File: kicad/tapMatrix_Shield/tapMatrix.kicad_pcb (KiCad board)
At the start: 2 copper layers, 121.9 x 80 mm, 24 parts, among them IC1 DS1307, P7 SPKR, U1 APE8865N-33-HF-3, U2 MCP4921-E/SN, U3 74LS125, U4 TL072

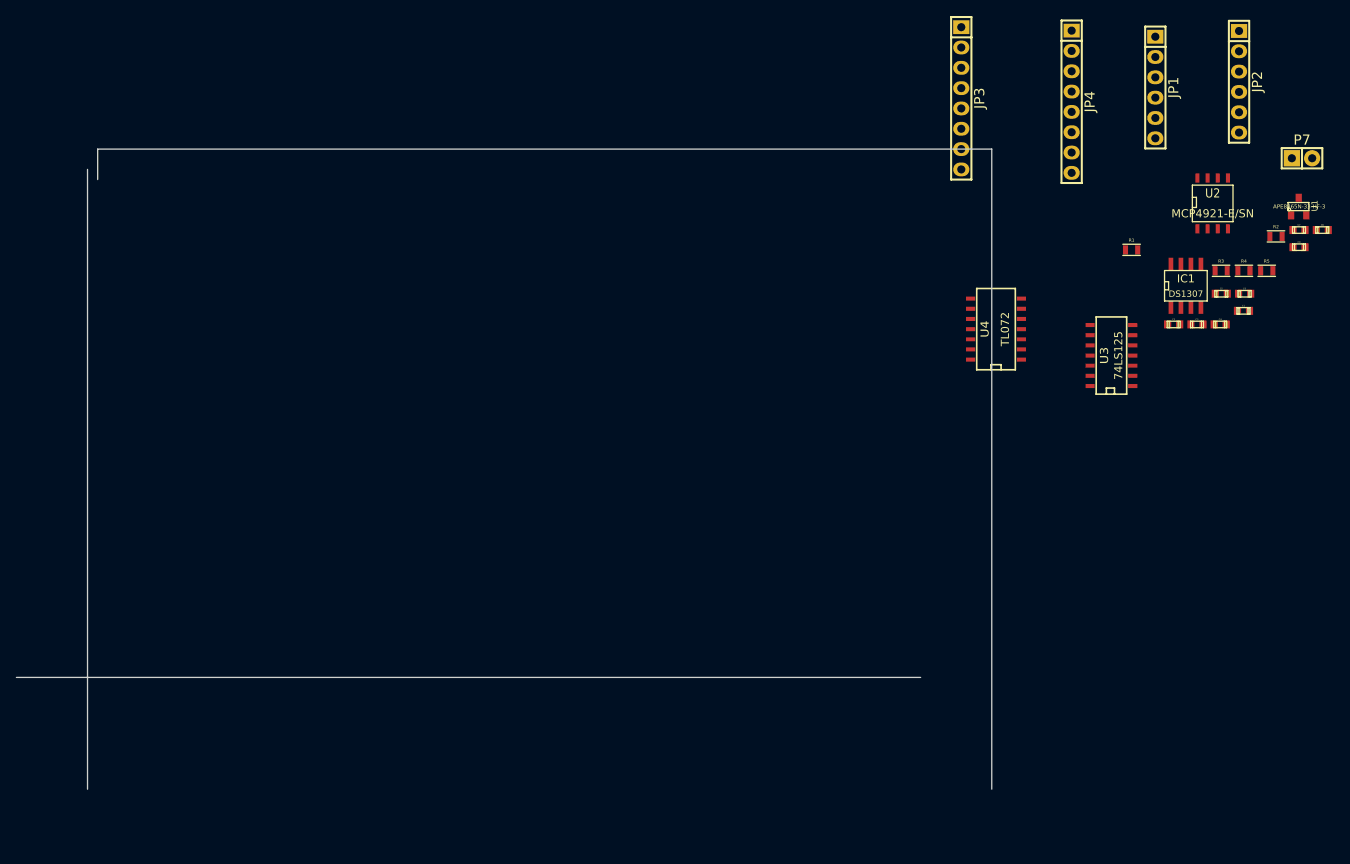
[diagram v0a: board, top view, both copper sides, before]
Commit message: added footprints for battery and ribbon sockets
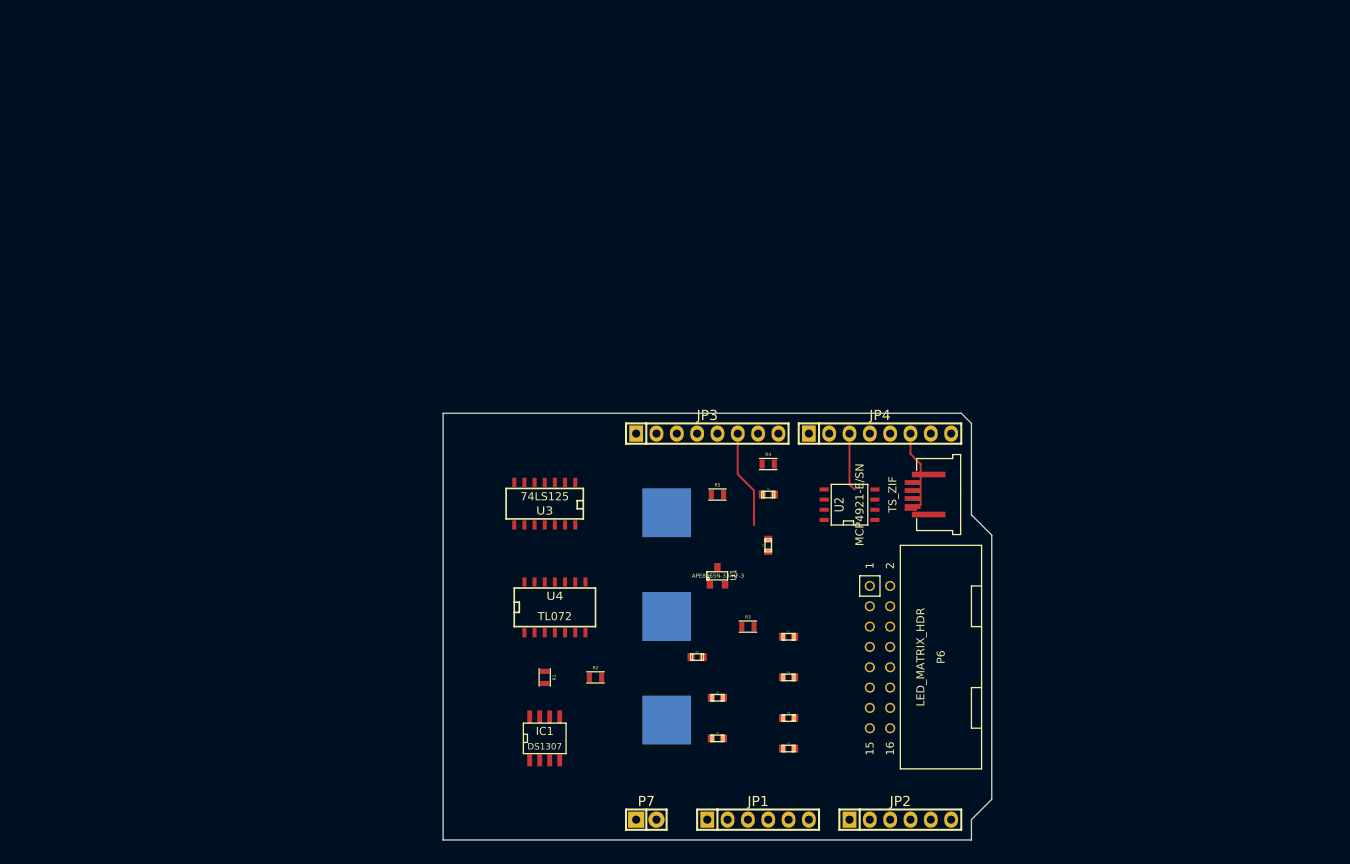
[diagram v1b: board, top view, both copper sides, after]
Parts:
- added BT1: BATTERY, tapmatrix:CR2032, B.Cu at (158.8, 111.8)
- added P5: TS_ZIF, tapmatrix:SFW4R­5STE1LF, F.Cu at (190.5, 96.5)
- added P6: LED_MATRIX_HDR, tapmatrix:5103310­-3, F.Cu at (185.4, 116.8)
- moved P7 116.4 mm to (156.2, 137.2)
- moved JP1 104.1 mm to (170.2, 137.2), turned to 0 degrees
- moved JP2 101.5 mm to (188.0, 137.2), turned to 0 degrees
- moved R2 101.4 mm to (149.9, 119.4)
- moved IC1 98.1 mm to (143.5, 127.0)
- moved C9 95.2 mm to (165.1, 127.0)
- moved R1 90.8 mm to (143.5, 119.4), turned to 270 degrees
- moved U1 86.1 mm to (165.1, 106.7)
- moved C6 83.0 mm to (165.1, 121.9)
- moved C5 79.7 mm to (162.6, 116.8)
- moved C7 77.2 mm to (171.4, 102.9), turned to 90 degrees
- moved C8 76.7 mm to (171.4, 96.5)
- moved R5 74.1 mm to (165.1, 96.5)
- moved R3 74.0 mm to (168.9, 113.0)
- moved U3 73.1 mm to (143.5, 97.8), turned to 180 degrees
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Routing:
- net /SD_CS: track 0.00 -> 12.3 mm
- net /XM: track 0.00 -> 9.04 mm
- net /DAC_LAT: track 0.00 -> 7.25 mm
- net /DAC_CS: track 0.00 -> 2.54 mm
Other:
- board size 121.9 x 80 mm -> 68.6 x 53.3 mm
- board text added: "3.3V"
- board text added: "5V"
- board text added: "Aref"
- board text added: "GND"
- board text added: "INT0"
- board text added: "INT1/PWM"
- board text added: "IOref"
- board text added: "MISO"
- board text added: "MOSI"
- board text added: "MOSI/PWM"
- board text added: "PWM"
- board text added: "RST"
- board text added: "Rx"
- board text added: "SCK"
- board text added: "SCK/LED"
- board text added: "SCL"
- board text added: "SDA"
- board text added: "SS/PWM"
- board text added: "Tx"
- board text added: "VTG"
- board text added: "Vin"

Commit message: created power and signal netclasses, updated design rules for oshpark
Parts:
- moved BT1 5.08 mm to (153.7, 111.8)
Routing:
- net /SD_CS: track 12.3 -> 0.00 mm
- net /DAC_LAT: track 7.25 -> 0.00 mm
- net /XM: track 9.04 -> 2.17 mm
- net /DAC_CS: track 2.54 -> 0.00 mm
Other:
- net class Power added: clearance 0.381, trace_width 0.762, via_dia 1.27, via_drill 0.889
- net class Signal added: clearance 0.1524, trace_width 0.254, via_dia 0.889, via_drill 0.635
- rule trace_min: 0.254 -> 0.1524
- rule via_min_drill: 0.508 -> 0.3302
- rule via_min_size: 0.889 -> 0.508
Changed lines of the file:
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@@
     (thickness 1.6)
     (drawings 96)
-    (tracks 10)
+    (tracks 2)
     (zones 0)
     (modules 27)
@@
   (setup
     (last_trace_width 0.254)
+    (user_trace_width 0.254)
+    (user_trace_width 0.3556)
+    (user_trace_width 0.508)
     (trace_clearance 0.254)
     (zone_clearance 0.508)
     (zone_45_only no)
-    (trace_min 0.254)
+    (trace_min 0.1524)
     (segment_width 0.2)
     (edge_width 0.1)
     (via_size 0.889)
     (via_drill 0.635)
-    (via_min_size 0.889)
-    (via_min_drill 0.508)
+    (via_min_size 0.508)
+    (via_min_drill 0.3302)
     (uvia_size 0.508)
     (uvia_drill 0.127)
     (uvias_allowed no)
-    (uvia_min_size 0.508)
-    (uvia_min_drill 0.127)
+    (uvia_min_size 0.381)
+    (uvia_min_drill 0.0127)
     (pcb_text_width 0.3)
     (pcb_text_size 1.5 1.5)
@@
     (uvia_dia 0.508)
     (uvia_drill 0.127)
+  )
+  (net_class Power ""
+    (clearance 0.381)
+    (trace_width 0.762)
+    (via_dia 1.27)
+    (via_drill 0.889)
+    (uvia_dia 0.508)
+    (uvia_drill 0.127)
     (add_net +3.3V)
     (add_net +5V)
+  )
+  (net_class Signal ""
+    (clearance 0.1524)
+    (trace_width 0.254)
+    (via_dia 0.889)
+    (via_drill 0.635)
+    (uvia_dia 0.508)
+    (uvia_drill 0.127)
     (add_net /CS)
     (add_net /DAC_CS)
@@
   )
   (module tapmatrix:CR2032 (layer B.Cu)
-    (at 158.75 111.76 270)
+    (at 153.67 111.76 270)
     (fp_text reference BT1 (at 0 -13.97 270) (layer B.SilkS)
       (effects (font (size 1 1) (thickness 0.15)) (justify mirror))
@@
   (module tapmatrix:SFW4R­5STE1LF (layer F.Cu)
     (at 190.5 96.52 90)
+    (clearance 0.1524)
     (fp_text reference P5 (at 0 7.5 90) (layer F.SilkS) hide
       (effects (font (size 1 1) (thickness 0.15)))
@@
   (gr_line (start 0 0) (end 66.04 0) (layer Dwgs.User) (width 0.1))
   (gr_line (start 0 0) (end 0 -53.34) (layer Dwgs.User) (width 0.1))
+  (segment (start 189.865 98.425) (end 188.595 98.425) (width 0.254) (layer F.Cu) (net 17))
   (segment (start 190.5 97.79) (end 189.865 98.425) (width 0.254) (layer F.Cu) (net 17))
-  (segment (start 190.5 92.71) (end 190.5 97.79) (width 0.254) (layer F.Cu) (net 17))
-  (segment (start 189.865 98.425) (end 188.595 98.425) (width 0.254) (layer F.Cu) (net 17))
-  (segment (start 189.23 91.44) (end 190.5 92.71) (width 0.254) (layer F.Cu) (net 17))
-  (segment (start 167.64 88.9) (end 167.64 93.98) (width 0.254) (layer F.Cu) (net 25))
-  (segment (start 169.672 96.012) (end 169.672 100.33) (width 0.254) (layer F.Cu) (net 25))
-  (segment (start 167.64 93.98) (end 169.672 96.012) (width 0.254) (layer F.Cu) (net 25))
-  (segment (start 181.61 88.9) (end 181.61 95.25) (width 0.254) (layer F.Cu) (net 30))
-  (segment (start 181.61 95.25) (end 182.245 95.885) (width 0.254) (layer F.Cu) (net 30))
-  (segment (start 189.23 88.9) (end 189.23 91.44) (width 0.254) (layer F.Cu) (net 33))
 )

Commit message: add microsd module
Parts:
- added U5: SD_CARD, tapmatrix:114-00841-68, F.Cu at (134.6, 87.6)
- moved P5 56.8 mm to (147.3, 133.3), turned to 0 degrees
- moved U3 14.0 mm to (157.5, 99.1), turned to 270 degrees
- moved R2 13.7 mm to (142.2, 108.0), turned to 270 degrees
- moved U4 12.8 mm to (157.5, 111.8), turned to 270 degrees
- moved R1 12.5 mm to (138.4, 108.0), turned to 0 degrees
- moved IC1 10.9 mm to (139.7, 116.8)
- moved U1 2.54 mm to (167.6, 106.7), turned to 180 degrees
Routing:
- net /XM: track 2.17 -> 0.00 mm
- net (no net): track 0.00 -> 2.17 mm

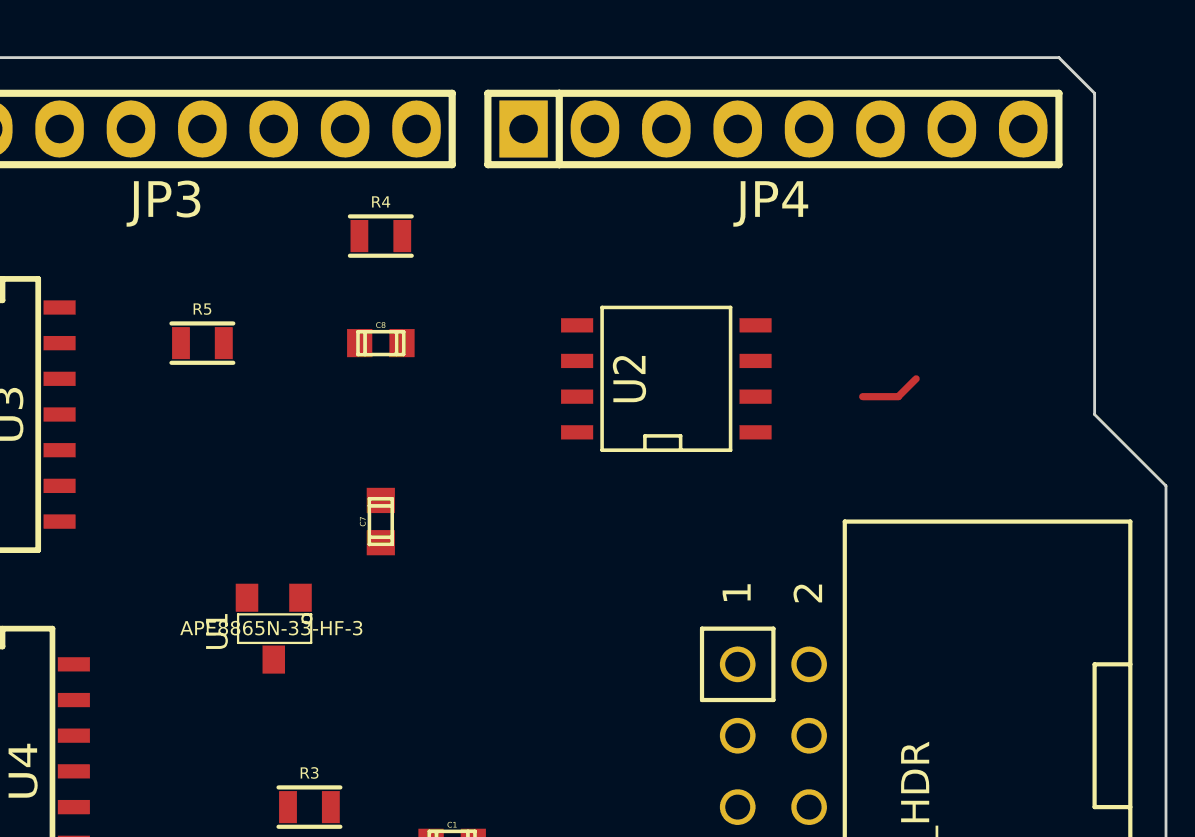
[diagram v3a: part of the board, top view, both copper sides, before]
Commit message: begin routing pcb
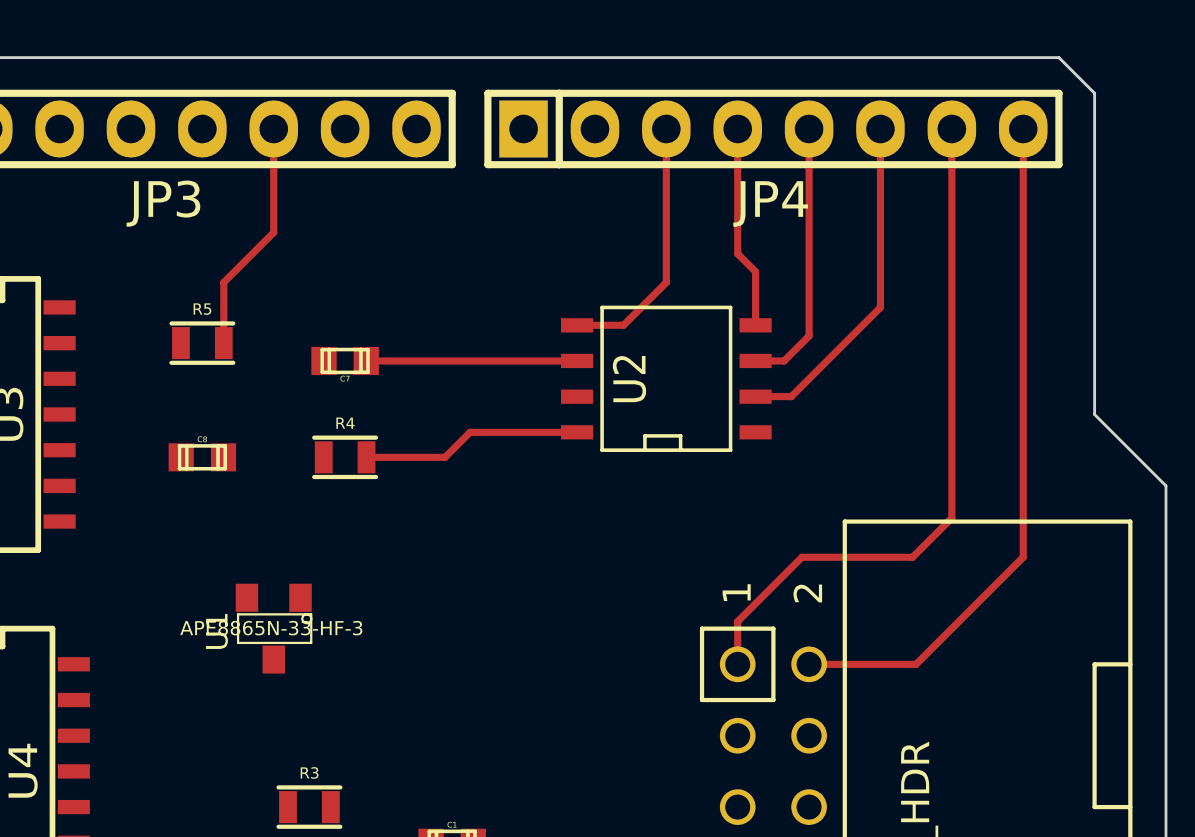
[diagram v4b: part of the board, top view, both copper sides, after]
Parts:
- moved R4 7.98 mm to (170.2, 100.6)
- moved C8 7.54 mm to (165.1, 100.6)
- moved C7 5.85 mm to (170.2, 97.2), turned to 180 degrees
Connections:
- net +3.3V renamed VCC
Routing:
- net /MATRIX_CS: track 0.00 -> 24.5 mm
- net /MATRIX_CLK: track 0.00 -> 24.4 mm
- net /DAC_CS: track 0.00 -> 12.1 mm
- net /DAC_SCK: track 0.00 -> 9.64 mm
- net /DAC_LAT: track 0.00 -> 9.27 mm
- net /SD_CS: track 0.00 -> 8.36 mm
- net Net-(R4-Pad2): track 0.00 -> 7.86 mm
- net Net-(C7-Pad2): track 0.00 -> 7.50 mm
- net /DAC_DI: track 0.00 -> 7.25 mm
- net (no net): track 2.17 -> 0.00 mm

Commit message: continue routing
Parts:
- moved C9 12.7 mm to (154.9, 119.4), turned to 180 degrees
- moved C5 3.86 mm to (166.4, 116.2)
- moved C6 2.84 mm to (166.4, 119.4)
- moved C2 2.16 mm to (174.0, 126.1)
- moved C3 1.90 mm to (174.0, 122.6)
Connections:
- U3 pad 6: /MISO -> /DATA_IN
- U5 pad 3: /MOSI -> /DATA_IN
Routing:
- net /I2C_SCL: track 0.00 -> 75.6 mm, vias 0 -> 2
- net VCC: track 0.00 -> 69.2 mm, vias 0 -> 2
- net /I2C_SDA: track 0.00 -> 68.6 mm
- net /YP: track 0.00 -> 50.0 mm
- net /XM: track 0.00 -> 48.7 mm
- net /YM: track 0.00 -> 47.6 mm
- net /XP: track 0.00 -> 47.1 mm, vias 0 -> 1
- net /MATRIX_DATA: track 0.00 -> 32.7 mm, vias 0 -> 2
- net /MATRIX_WR: track 0.00 -> 31.4 mm, vias 0 -> 2
- net Net-(BT1-Pad1): track 0.00 -> 31.2 mm, vias 0 -> 1
- net /MISO: track 0.00 -> 29.0 mm, vias 0 -> 1
- net /CS: track 0.00 -> 26.9 mm
- net Net-(C9-Pad2): track 0.00 -> 25.4 mm, vias 0 -> 2
- net /DATA_IN: track 0.00 -> 20.7 mm
- net /SCLK: track 0.00 -> 20.1 mm
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- added copper zone on F.Cu, net +5V
- added copper zone on B.Cu, net GND

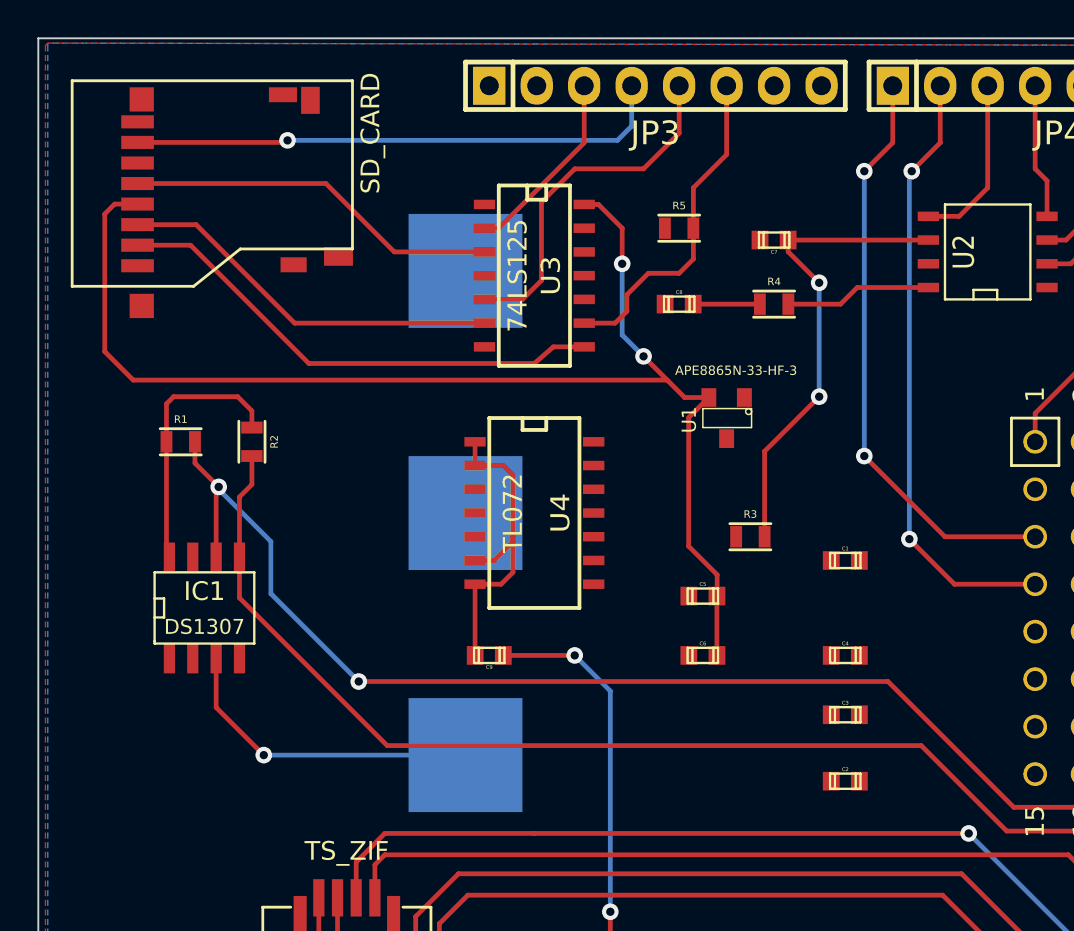
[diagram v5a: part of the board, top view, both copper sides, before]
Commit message: complete first attempt at routing
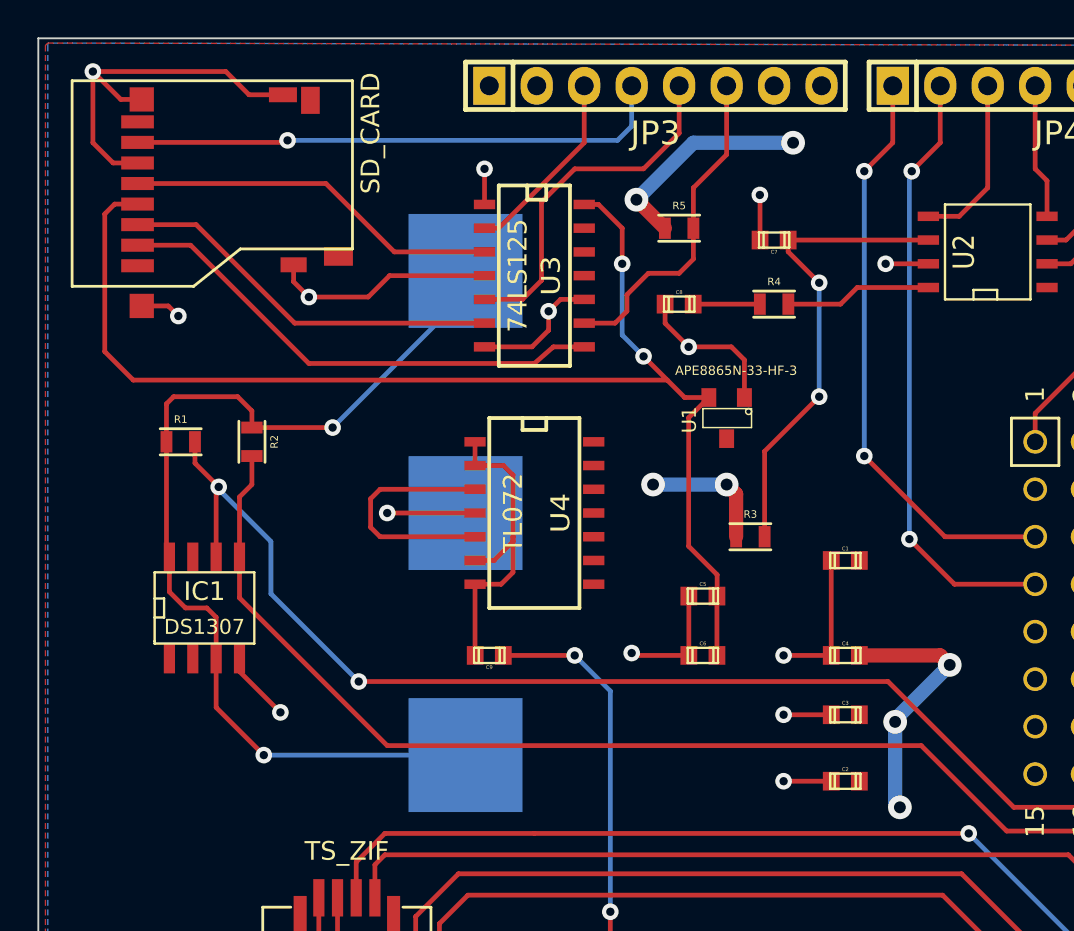
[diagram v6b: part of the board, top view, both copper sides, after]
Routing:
- net GND: track 0.00 -> 83.9 mm, vias 0 -> 14
- net +5V: track 0.00 -> 32.7 mm, vias 0 -> 7
- net Net-(BT1-Pad1): track 31.2 -> 54.0 mm, vias 1 -> 2
- net Net-(RV1-Pad2): track 0.00 -> 13.1 mm

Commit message: removed volume pot; created gerber files
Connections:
- net VCC renamed +3.3V
- U4 pad 3: Net-(RV1-Pad2) -> Net-(C8-Pad1)
- U4 pad 5: Net-(RV1-Pad2) -> Net-(C8-Pad1)
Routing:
- net Net-(C8-Pad1): track 3.57 -> 47.6 mm, vias 0 -> 2
- net Net-(RV1-Pad2): track 13.1 -> 0.00 mm
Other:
- board text added: "(c) 2014 Responsive Devices Inc"
- board text added: "tapMatrix Shield 0.1 August 2014"
